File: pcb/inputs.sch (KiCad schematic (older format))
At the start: 61 parts, among them U11 MPXA6115AC6U, U4 MAX9926UAEE+, U6 MPX4250AP

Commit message: update
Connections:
- net MAT-CPU-Signal renamed SPR-CPU-Signal
- net MAT-Sensor renamed SPR-Sensor
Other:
- note added: "Spare ADC Input"
- note removed: "Manifold Air Temperature"

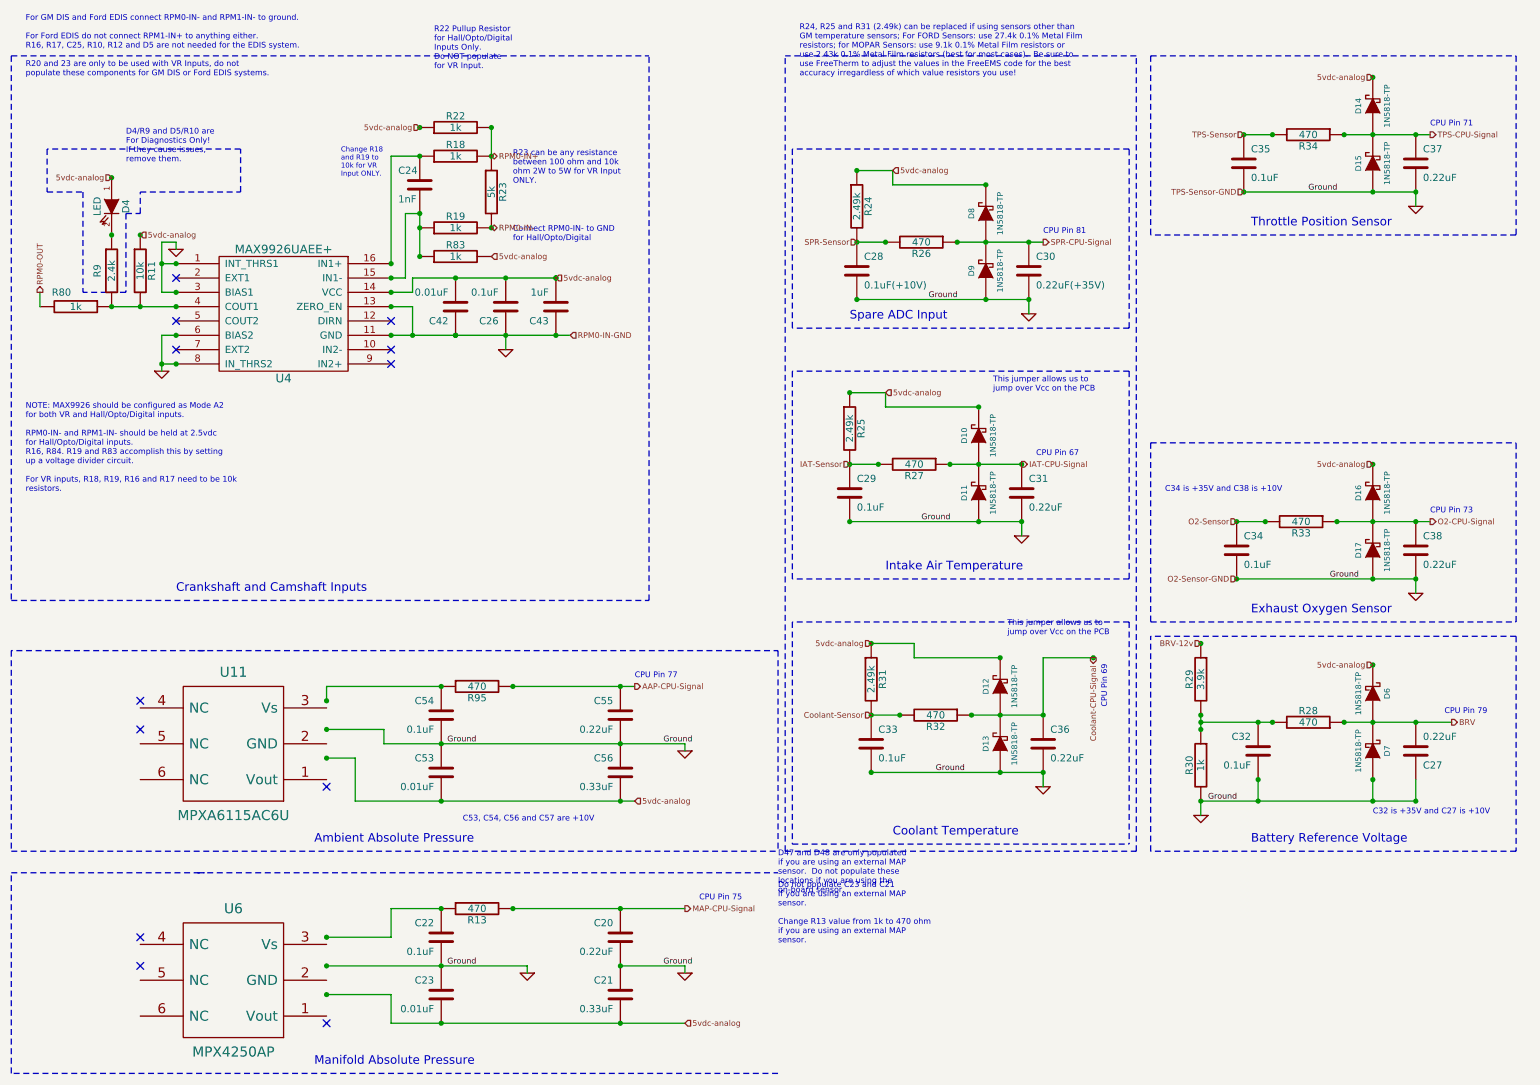
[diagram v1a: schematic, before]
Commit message: schematics update
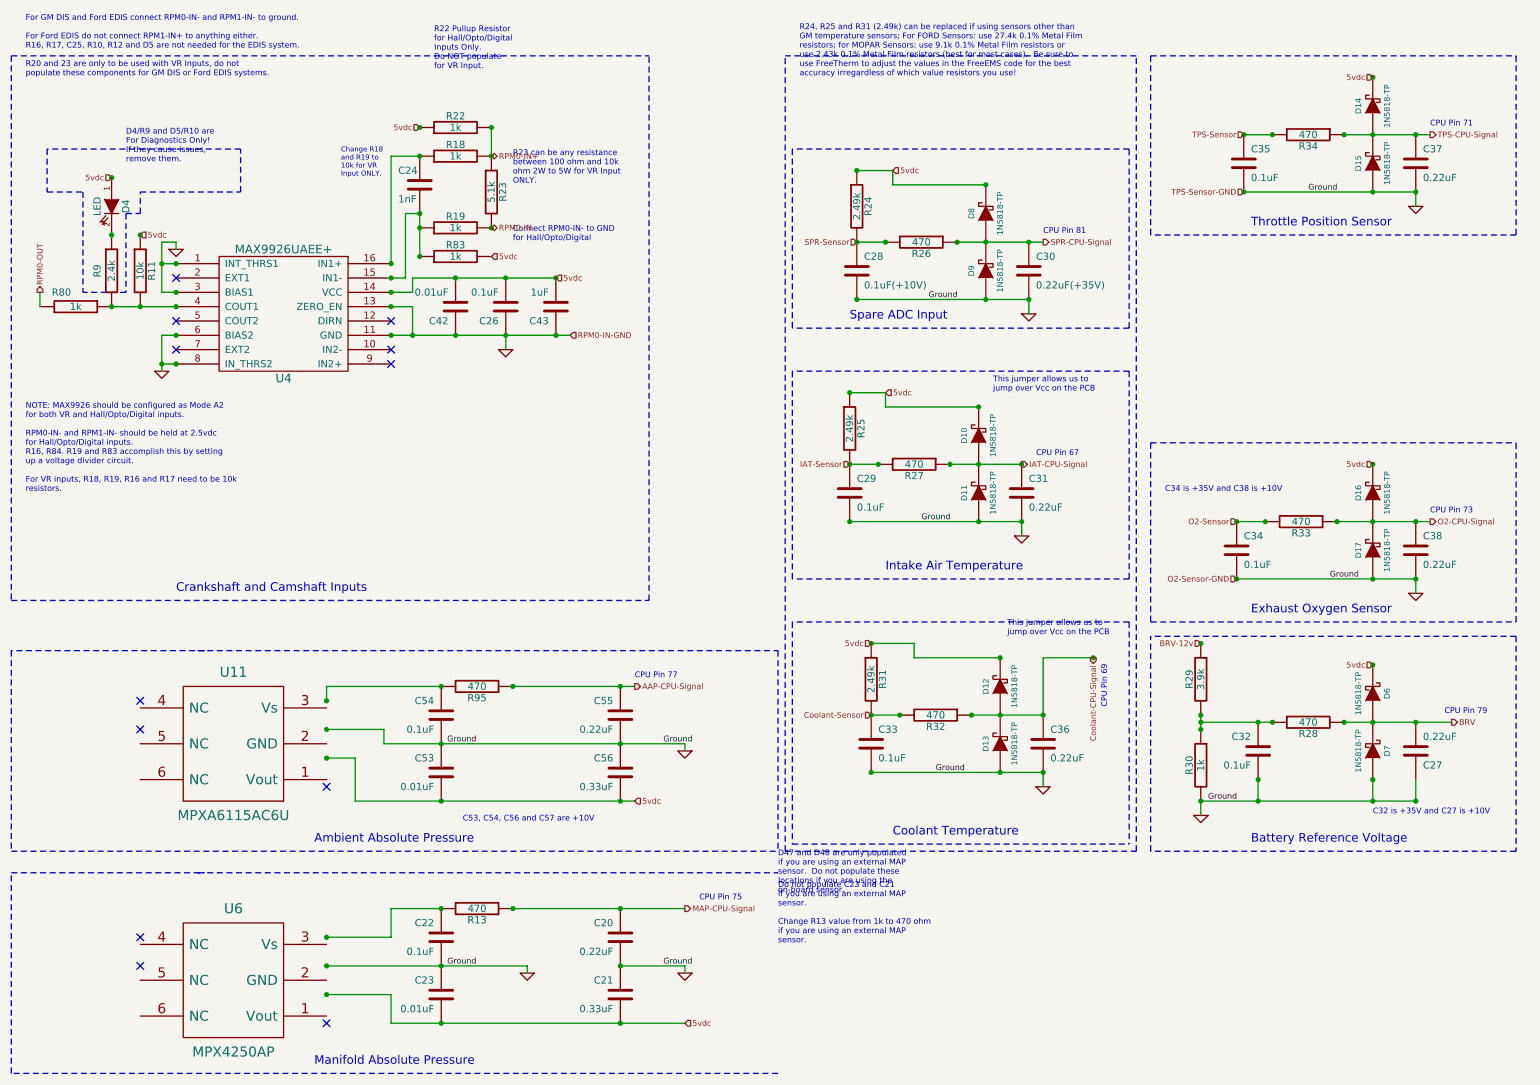
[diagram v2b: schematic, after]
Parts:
- R23: value 5k -> 5.1k
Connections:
- net BRV: now also R28.2; no longer R28.1
- net at C32.1, R29.2, R30.1: now also R28.1; no longer R28.2
- net 5vdc-analog renamed 5vdc

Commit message: MPX4250 footprint
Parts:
- removed U11: MPXA6115AC6U, symbol MPXA4250AP
- added U11: MPXA6115AC6U, ~, symbol MPXA6115AC6U
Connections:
- net 5vdc: now also U6.3 (Vs), U11.2 (Vin)
- net GND: now also U6.2 (GND), U11.3 (GND)
- net at C22.1, R13.1: now also U6.1 (Vout)
- net at C54.1, R95.1: now also U11.4 (Vout)
- no-connect marks 12 -> 14
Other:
- moved on the sheet: U6
